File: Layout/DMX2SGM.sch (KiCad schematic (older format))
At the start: 32 parts, among them J1 AVR-ISP-6, J2 Conn_01x03, J3 Conn_01x03, J4 Conn_01x03, J5 Conn_01x03, SW1 BD09AV, U1 ATtiny1634, U2 485, U3 6N137, U4 REE-0505S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

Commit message: Bugfixes & Cleanup
Code cleanup, Fixing a few bugs, General code optimations
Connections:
- net +5VD: now also J1.2 (VCC)
- net ICSP_SCL: now also U1.17 (PC0)
- no-connect marks 3 -> 1
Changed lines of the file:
@@
 Title "DMX2SGM"
 Date "13.09.2019"
-Rev "0.2"
+Rev "3"
 Comp "Gabs'e"
 Comment1 "CC BY-NC-SA"
@@
 	3950 4900 3950 5050
 Wire Wire Line
-	3050 3900 2700 3900
+	3050 3900 2900 3900
 Wire Wire Line
 	2700 4100 3050 4100
@@
 Wire Wire Line
 	1850 7250 2000 7250
-NoConn ~ 1400 6050
 Wire Wire Line
 	7550 5450 7450 5450
@@
 	1    2150 7250
 	0    1    1    0
-$EndComp
-$Comp
-L DMX2SGM-rescue:AVR-ISP-6-Connector J1
-U 1 1 5D7D64E6
-P 1500 6550
-F 0 "J1" H 1221 6646 50  0000 R CNN
-F 1 "AVR-ISP-6" H 1221 6555 50  0000 R CNN
-F 2 "Connector_PinHeader_2.54mm:PinHeader_2x03_P2.54mm_Vertical" V 1250 6600 50  0001 C CNN
-F 3 "https://cdn.amphenol-icc.com/media/wysiwyg/files/drawing/67996.pdf" H 225 6000 50  0001 C CNN
-F 4 "TME" H 1500 6550 50  0001 C CNN "Vendor"
-F 5 "67996-206HLF" H 1500 6550 50  0001 C CNN "MPN"
-F 6 "AMPHENOL" H 1500 6550 50  0001 C CNN "Manuf"
-F 7 "67996-206HLF" H 1500 6550 50  0001 C CNN "VPN"
-	1    1500 6550
-	1    0    0    -1
 $EndComp
 $Comp
@@
 Wire Wire Line
 	7050 4000 7150 4000
-NoConn ~ 2700 3800
 Wire Wire Line
 	6900 3200 6900 3300
@@
 	1    0    0    -1
 $EndComp
-Wire Bus Line
-	5300 2150 5300 3100
-Wire Bus Line
-	3600 2150 3600 3100
 Wire Wire Line
 	6050 6200 5800 6200
@@
 	0    1    1    0
 $EndComp
+Wire Wire Line
+	2700 3800 2900 3800
+Wire Wire Line
+	2900 3800 2900 3900
+Connection ~ 2900 3900
+Wire Wire Line
+	2900 3900 2700 3900
+$Comp
+L DMX2SGM-rescue:AVR-ISP-6-Connector J1
+U 1 1 5D7D64E6
+P 1500 6550
+F 0 "J1" H 1221 6646 50  0000 R CNN
+F 1 "AVR-ISP-6" H 1221 6555 50  0000 R CNN
+F 2 "Connector_PinHeader_2.54mm:PinHeader_2x03_P2.54mm_Vertical" V 1250 6600 50  0001 C CNN
+F 3 "https://cdn.amphenol-icc.com/media/wysiwyg/files/drawing/67996.pdf" H 225 6000 50  0001 C CNN
+F 4 "TME" H 1500 6550 50  0001 C CNN "Vendor"
+F 5 "67996-206HLF" H 1500 6550 50  0001 C CNN "MPN"
+F 6 "AMPHENOL" H 1500 6550 50  0001 C CNN "Manuf"
+F 7 "67996-206HLF" H 1500 6550 50  0001 C CNN "VPN"
+	1    1500 6550
+	1    0    0    -1
+$EndComp
+$Comp
+L power:+5VD #PWR?
+U 1 1 6062247A
+P 1400 5900
+F 0 "#PWR?" H 1400 5750 50  0001 C CNN
+F 1 "+5VD" H 1415 6073 50  0000 C CNN
+F 2 "" H 1400 5900 50  0001 C CNN
+F 3 "" H 1400 5900 50  0001 C CNN
+	1    1400 5900
+	1    0    0    -1
+$EndComp
+Wire Wire Line
+	1400 5900 1400 6050
+Wire Bus Line
+	3600 2150 3600 3100
+Wire Bus Line
+	5300 2150 5300 3100
 $EndSCHEMATC

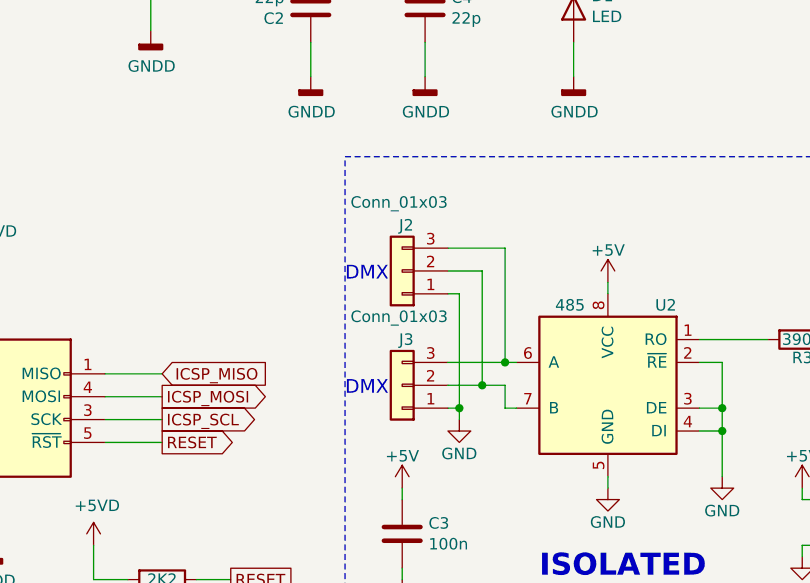
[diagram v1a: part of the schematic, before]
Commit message: Fix random reboot, fix OBOE, improve layout
Fix MCU randomly rebooting.
Fix DMX address DIP switch off-by-one-error.
Modify PCB for easier device assembly.
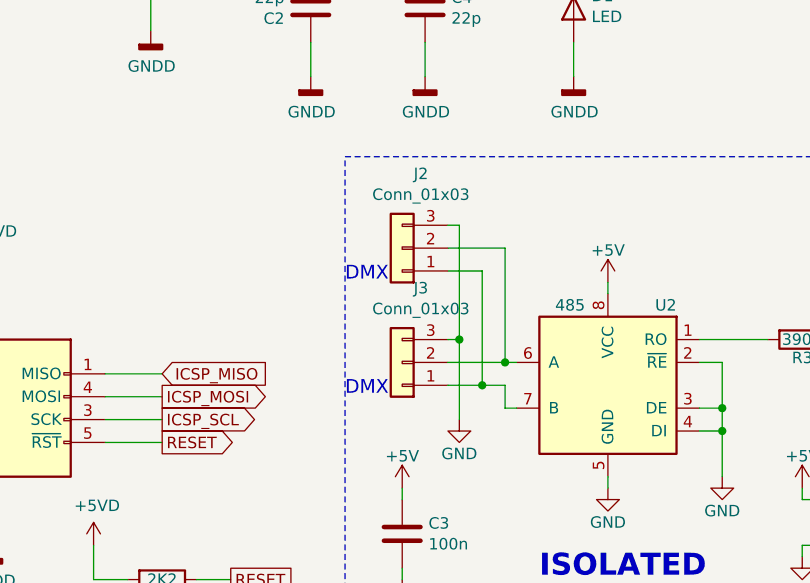
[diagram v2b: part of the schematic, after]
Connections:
- net GND: now also J2.3 (Pin_3), J3.3 (Pin_3); no longer J2.1 (Pin_1), J3.1 (Pin_1)
- net at J2.2 (Pin_2), J3.2 (Pin_2): now also U2.6 (A); no longer U2.7 (B)
- new net: J2.1 (Pin_1), J3.1 (Pin_1), U2.7 (B)
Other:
- moved on the sheet: J2, J3
